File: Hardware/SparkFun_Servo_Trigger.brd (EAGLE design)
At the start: 22.9 x 43.2 mm, 26 parts, among them U1 ATTINY84, Y1 16MHZ

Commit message: After engineering review
PCB is ready for QC checklist.
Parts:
- added LOGO3: SFE_LOGO_FLAME.2_INCH, SparkFun-Aesthetics:SFE_LOGO_FLAME_.2
- moved FRAME1 7.62 mm to (0.00, -19.1)
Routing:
- net A: track 19.9 -> 15.4 mm
- net POLSEL: track 24.2 -> 23.7 mm
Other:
- board text added: "0.13inch diam. Clears 4-40 screw"

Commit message: Updates based on checklist
Undoing pour under IC.
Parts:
- FRAME1: value FRAME-LETTER -> (none)
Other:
- board text removed: "Byron Jacquot"
- board text removed: "V10"
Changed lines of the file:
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@@
 <layer number="39" name="tKeepout" color="4" fill="11" visible="no" active="yes"/>
 <layer number="40" name="bKeepout" color="1" fill="11" visible="no" active="yes"/>
-<layer number="41" name="tRestrict" color="4" fill="10" visible="no" active="yes"/>
+<layer number="41" name="tRestrict" color="4" fill="10" visible="yes" active="yes"/>
 <layer number="42" name="bRestrict" color="1" fill="10" visible="no" active="yes"/>
 <layer number="43" name="vRestrict" color="2" fill="10" visible="no" active="yes"/>
@@
 <layer number="251" name="SMDround" color="12" fill="11" visible="no" active="no"/>
 <layer number="254" name="cooling" color="7" fill="1" visible="no" active="yes"/>
+<layer number="255" name="routoute" color="7" fill="1" visible="yes" active="yes"/>
 </layers>
 <board>
@@
 <wire x1="22.86" y1="43.18" x2="0" y2="43.18" width="0.2032" layer="20"/>
 <wire x1="0" y1="43.18" x2="0" y2="0.016" width="0.2032" layer="20"/>
-<text x="30.48" y="-19.05" size="1.778" layer="51" ratio="15">Byron Jacquot</text>
-<text x="4.952" y="2.444" size="1.27" layer="16" font="vector" ratio="15" rot="MR180">V10</text>
 <text x="11.43" y="31.75" size="1.778" layer="22" font="vector" ratio="15" rot="SMR270">Servo Trigger</text>
 <text x="5.334" y="29.226" size="2.54" layer="21" font="vector" ratio="15" align="bottom-center">A</text>
@@
 <text x="31.75" y="-7.62" size="1.778" layer="47" font="vector" ratio="15">0.13inch diam.
 Clears 4-40 screw</text>
+<rectangle x1="4.572" y1="14.732" x2="4.699" y2="17.018" layer="41"/>
+<rectangle x1="4.572" y1="15.875" x2="6.731" y2="16.002" layer="41"/>
 </plain>
 <attributes>
@@
 </autorouter>
 <elements>
-<element name="FRAME1" library="SparkFun-Aesthetics" package="CREATIVE_COMMONS" value="FRAME-LETTER" x="0" y="-19.05"/>
+<element name="FRAME1" library="SparkFun-Aesthetics" package="CREATIVE_COMMONS" value="" x="0" y="-19.05" smashed="yes">
+<attribute name="VERSION" value="V10" x="8.255" y="0.635" size="1.27" layer="16" font="vector" ratio="15" rot="SMR0"/>
+<attribute name="DESIGNER" value="Byron Jacquot" x="30.48" y="-19.05" size="1.778" layer="51"/>
+</element>
 <element name="R4" library="SparkFun-Resistors" package="0603-RES" value="10K" x="2.54" y="10.16" rot="R90">
 <attribute name="PROD_ID" value="RES-00824" x="2.54" y="10.16" size="1.778" layer="27" rot="R90" display="off"/>

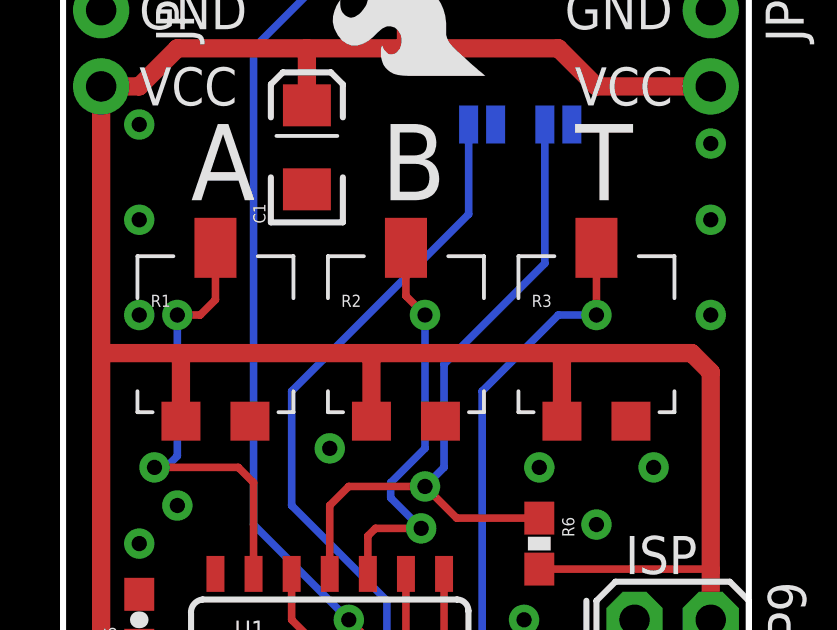
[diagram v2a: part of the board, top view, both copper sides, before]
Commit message: Adding test point off each trimpot
As per discussion with Bryon we decided to add a test point off of each
pot's ADC line in order to better automate production testing.
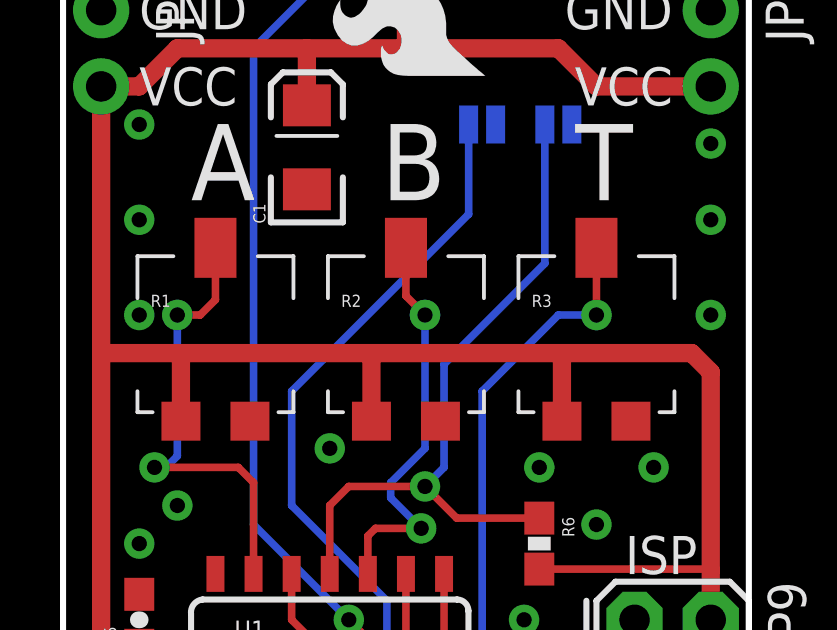
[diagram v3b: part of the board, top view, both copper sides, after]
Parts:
- added TP1, TP2, TP3: TEST-POINT3X4, SparkFun-Passives:PAD.03X.04
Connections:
- net A: now also TP1.P$1
- net B: now also TP2.P$1
- net T: now also TP3.P$1
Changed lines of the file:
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@@
 <layer number="23" name="tOrigins" color="15" fill="1" visible="yes" active="yes"/>
 <layer number="24" name="bOrigins" color="15" fill="1" visible="yes" active="yes"/>
-<layer number="25" name="tNames" color="7" fill="1" visible="yes" active="yes"/>
+<layer number="25" name="tNames" color="7" fill="1" visible="no" active="yes"/>
 <layer number="26" name="bNames" color="7" fill="1" visible="no" active="yes"/>
 <layer number="27" name="tValues" color="7" fill="1" visible="no" active="yes"/>
@@
 <layer number="39" name="tKeepout" color="4" fill="11" visible="no" active="yes"/>
 <layer number="40" name="bKeepout" color="1" fill="11" visible="no" active="yes"/>
-<layer number="41" name="tRestrict" color="4" fill="10" visible="yes" active="yes"/>
+<layer number="41" name="tRestrict" color="4" fill="10" visible="no" active="yes"/>
 <layer number="42" name="bRestrict" color="1" fill="10" visible="no" active="yes"/>
 <layer number="43" name="vRestrict" color="2" fill="10" visible="no" active="yes"/>
@@
 <layer number="45" name="Holes" color="7" fill="1" visible="yes" active="yes"/>
 <layer number="46" name="Milling" color="3" fill="1" visible="no" active="yes"/>
-<layer number="47" name="Measures" color="7" fill="1" visible="yes" active="yes"/>
+<layer number="47" name="Measures" color="7" fill="1" visible="no" active="yes"/>
 <layer number="48" name="Document" color="7" fill="1" visible="no" active="yes"/>
 <layer number="49" name="Reference" color="7" fill="1" visible="no" active="yes"/>
@@
 <layer number="251" name="SMDround" color="12" fill="11" visible="no" active="no"/>
 <layer number="254" name="cooling" color="7" fill="1" visible="no" active="yes"/>
-<layer number="255" name="routoute" color="7" fill="1" visible="yes" active="yes"/>
+<layer number="255" name="routoute" color="7" fill="1" visible="no" active="yes"/>
 </layers>
 <board>
@@
 <element name="JP4" library="SparkFun-Connectors" package="1X02_NO_SILK" value="M021X02_NO_SILK" x="21.59" y="35.56" rot="R270"/>
 <element name="LOGO3" library="SparkFun-Aesthetics" package="SFE_LOGO_FLAME_.2" value="SFE_LOGO_FLAME.2_INCH" x="14.351" y="33.02" rot="R90"/>
+<element name="TP1" library="SparkFun-Passives" package="PAD.03X.04" value="TEST-POINT3X4" x="3.81" y="25.4" rot="MR0"/>
+<element name="TP2" library="SparkFun-Passives" package="PAD.03X.04" value="TEST-POINT3X4" x="12.065" y="25.4" rot="MR0"/>
+<element name="TP3" library="SparkFun-Passives" package="PAD.03X.04" value="TEST-POINT3X4" x="17.78" y="25.4" rot="MR0"/>
 </elements>
 <signals>
@@
 <via x="11.43" y="9.525" extent="1-16" drill="0.508"/>
 <wire x1="11.43" y1="9.525" x2="12.065" y2="10.16" width="0.254" layer="16"/>
+<contactref element="TP3" pad="P$1"/>
 </signal>
 <signal name="B">
@@
 <wire x1="10.922" y1="19.812" x2="10.922" y2="19.304" width="0.254" layer="16"/>
 <wire x1="10.922" y1="19.304" x2="11.938" y2="18.288" width="0.254" layer="16"/>
+<contactref element="TP2" pad="P$1"/>
 </signal>
 <signal name="A">
@@
 <wire x1="5.08" y1="25.908" x2="4.572" y2="25.4" width="0.254" layer="1"/>
 <wire x1="4.572" y1="25.4" x2="3.81" y2="25.4" width="0.254" layer="1"/>
+<contactref element="TP1" pad="P$1"/>
 </signal>
 <signal name="BTN">
@@
 </signal>
 </signals>
+<errors>
+</errors>
 </board>
 </drawing>

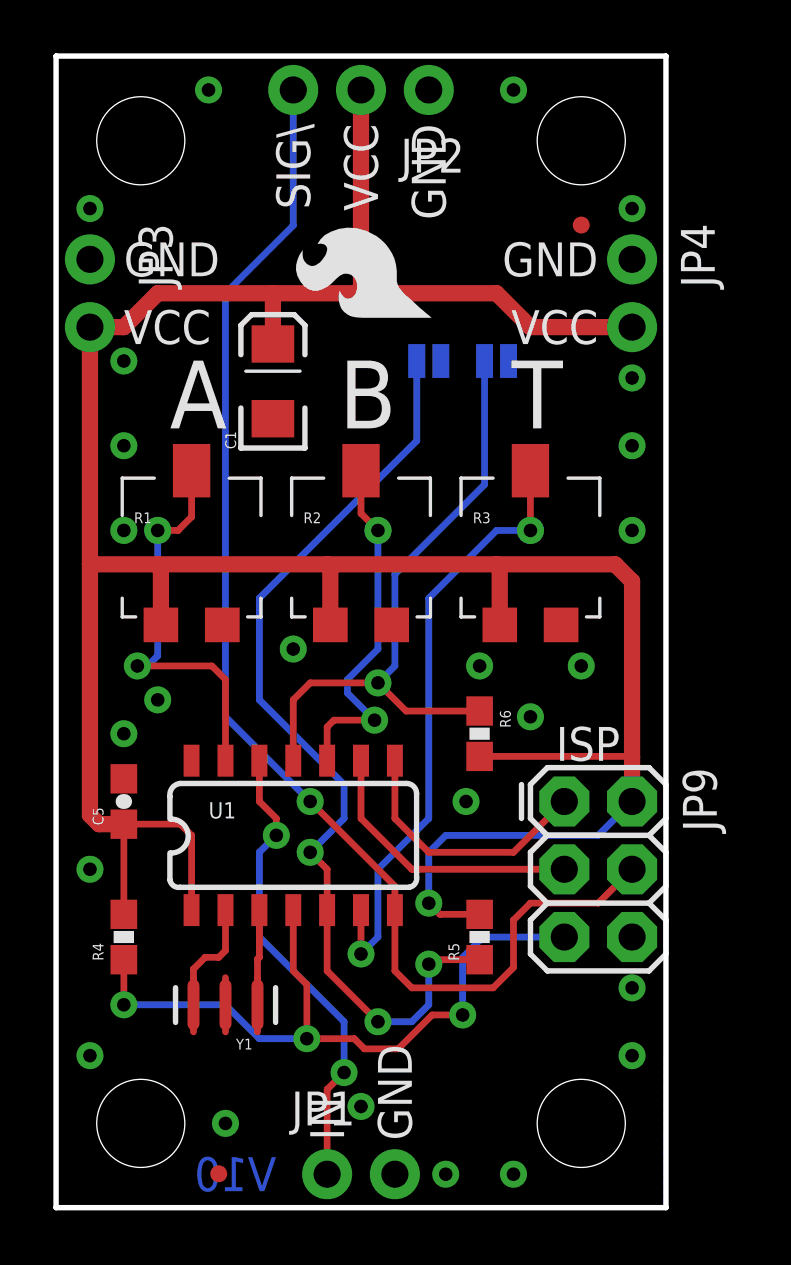
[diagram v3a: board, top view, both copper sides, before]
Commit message: changed micro fids to regular size
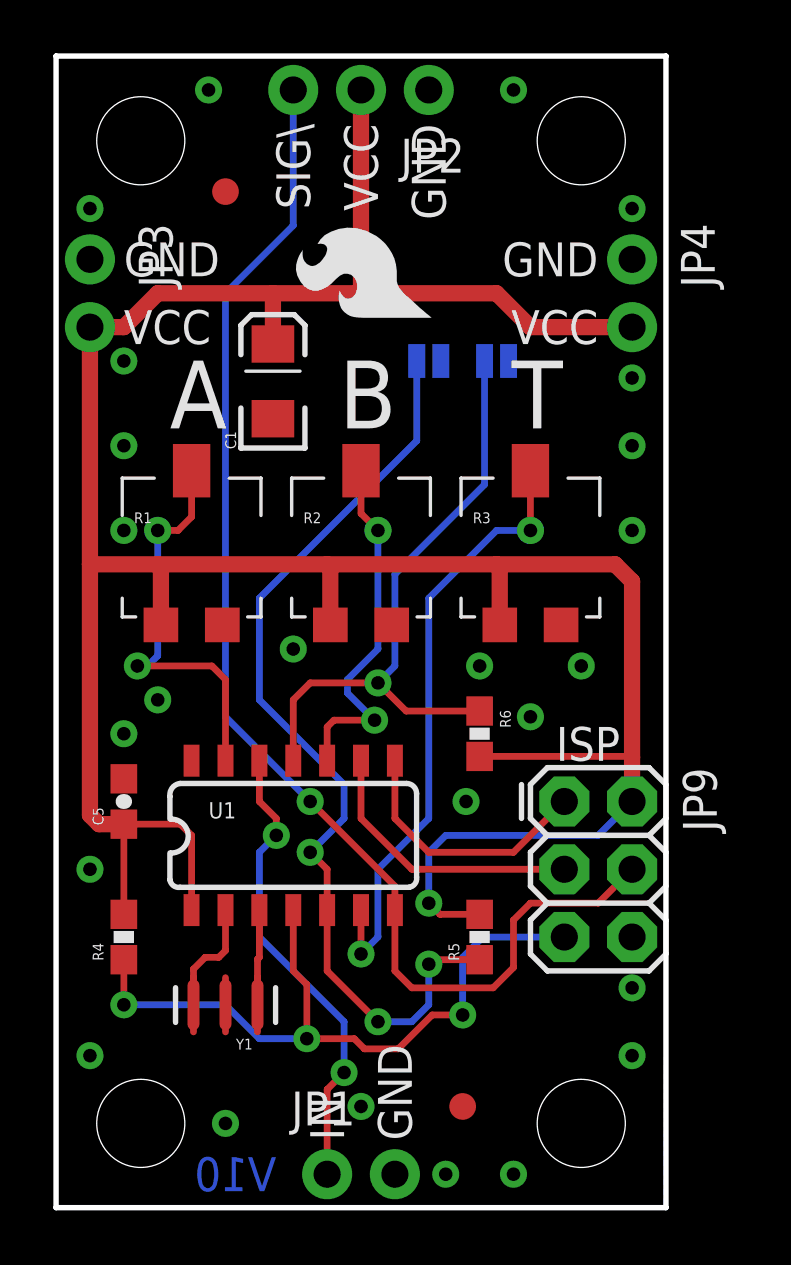
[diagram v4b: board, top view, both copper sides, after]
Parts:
- FID1, FID2: value FIDUCIALUFIDUCIAL -> FIDUCIAL1X2; device SparkFun-Aesthetics:MICRO-FIDUCIAL -> SparkFun-Aesthetics:FIDUCIAL-1X2
- moved FID1 36.8 mm to (6.35, 38.1)
- moved FID2 33.3 mm to (15.2, 3.81)

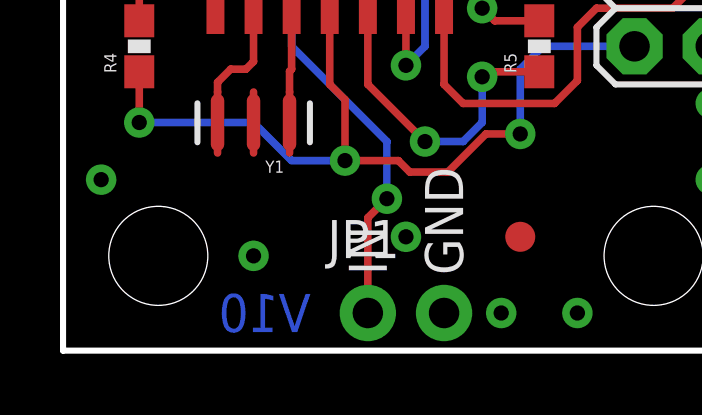
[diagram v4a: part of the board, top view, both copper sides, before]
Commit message: Checking in V1.1 revision
Adding silkscreen tickboxes for standard/continuous rotation.

Moving to "STANDARD" DRC.
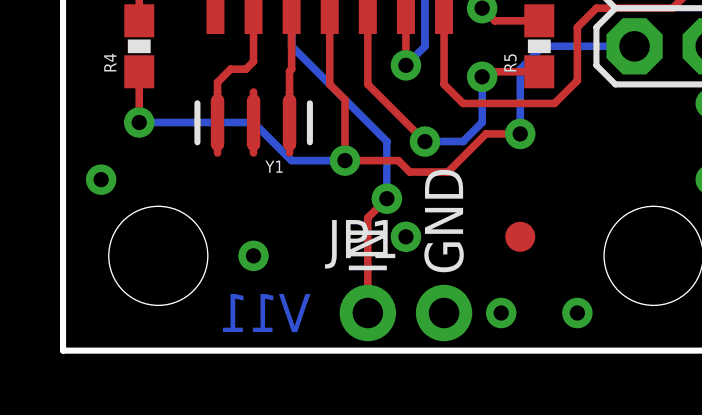
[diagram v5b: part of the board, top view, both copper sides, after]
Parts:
- moved LOGO2 3.18 mm to (6.35, 31.8)
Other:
- board text added: "Continuous Rotation"
- board text added: "Standard"
